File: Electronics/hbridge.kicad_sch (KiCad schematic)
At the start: 24 parts

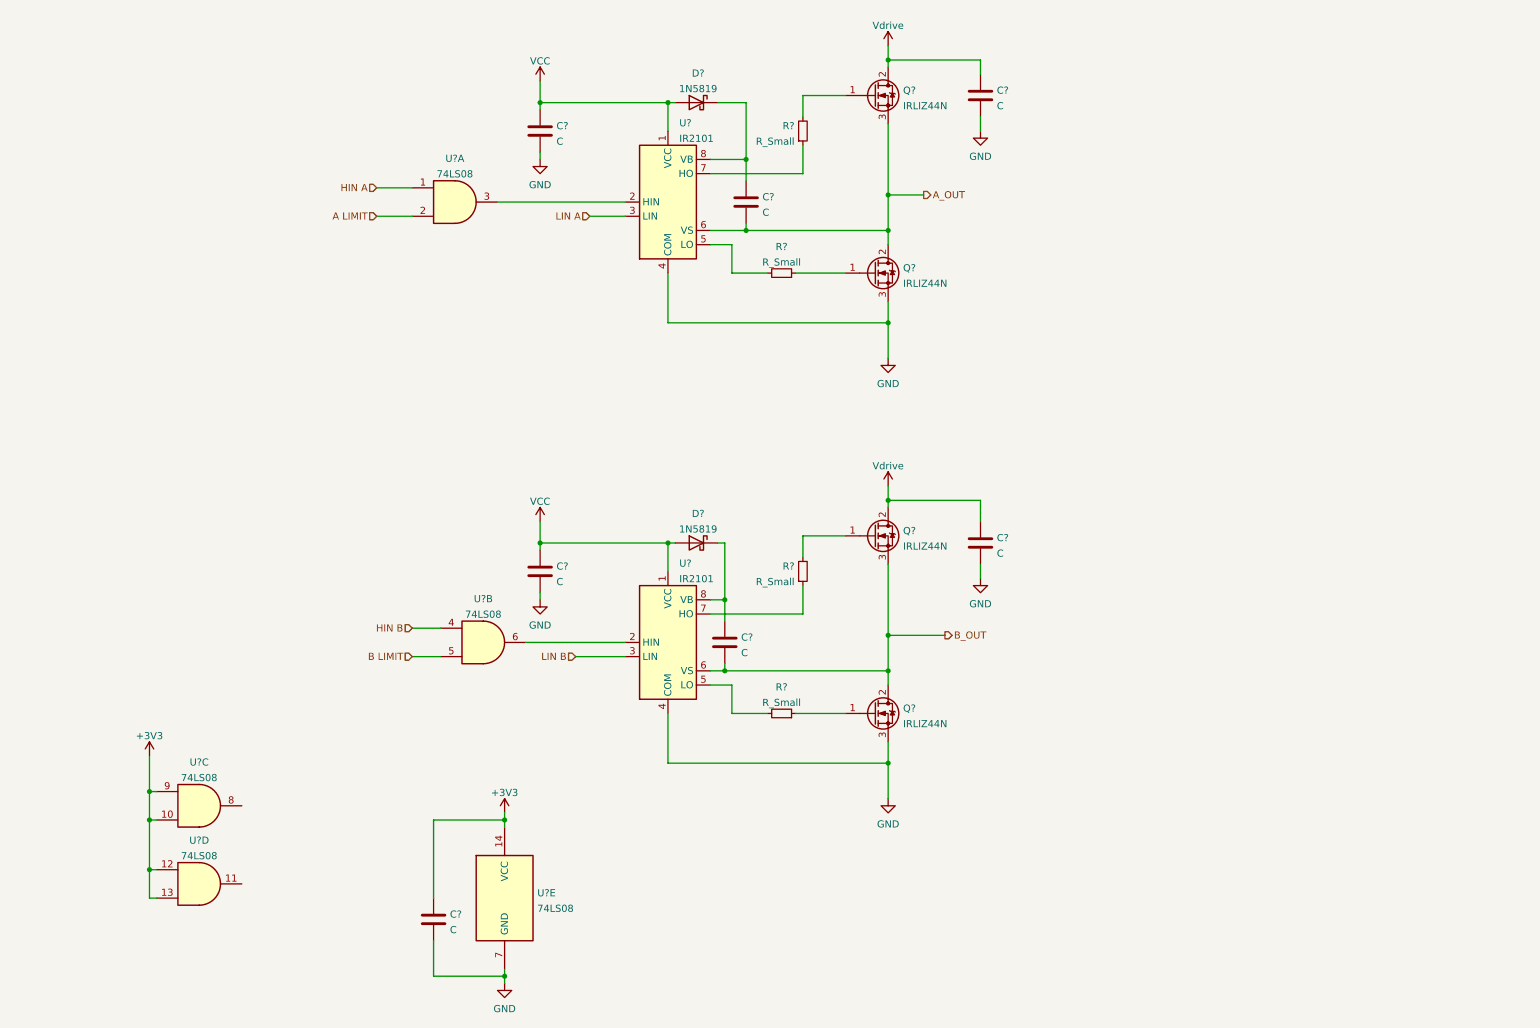
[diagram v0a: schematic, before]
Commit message: Added third half bridge for BLDC applications
Signed-off-by: Finder <aki.kuusela@findersee.fi>
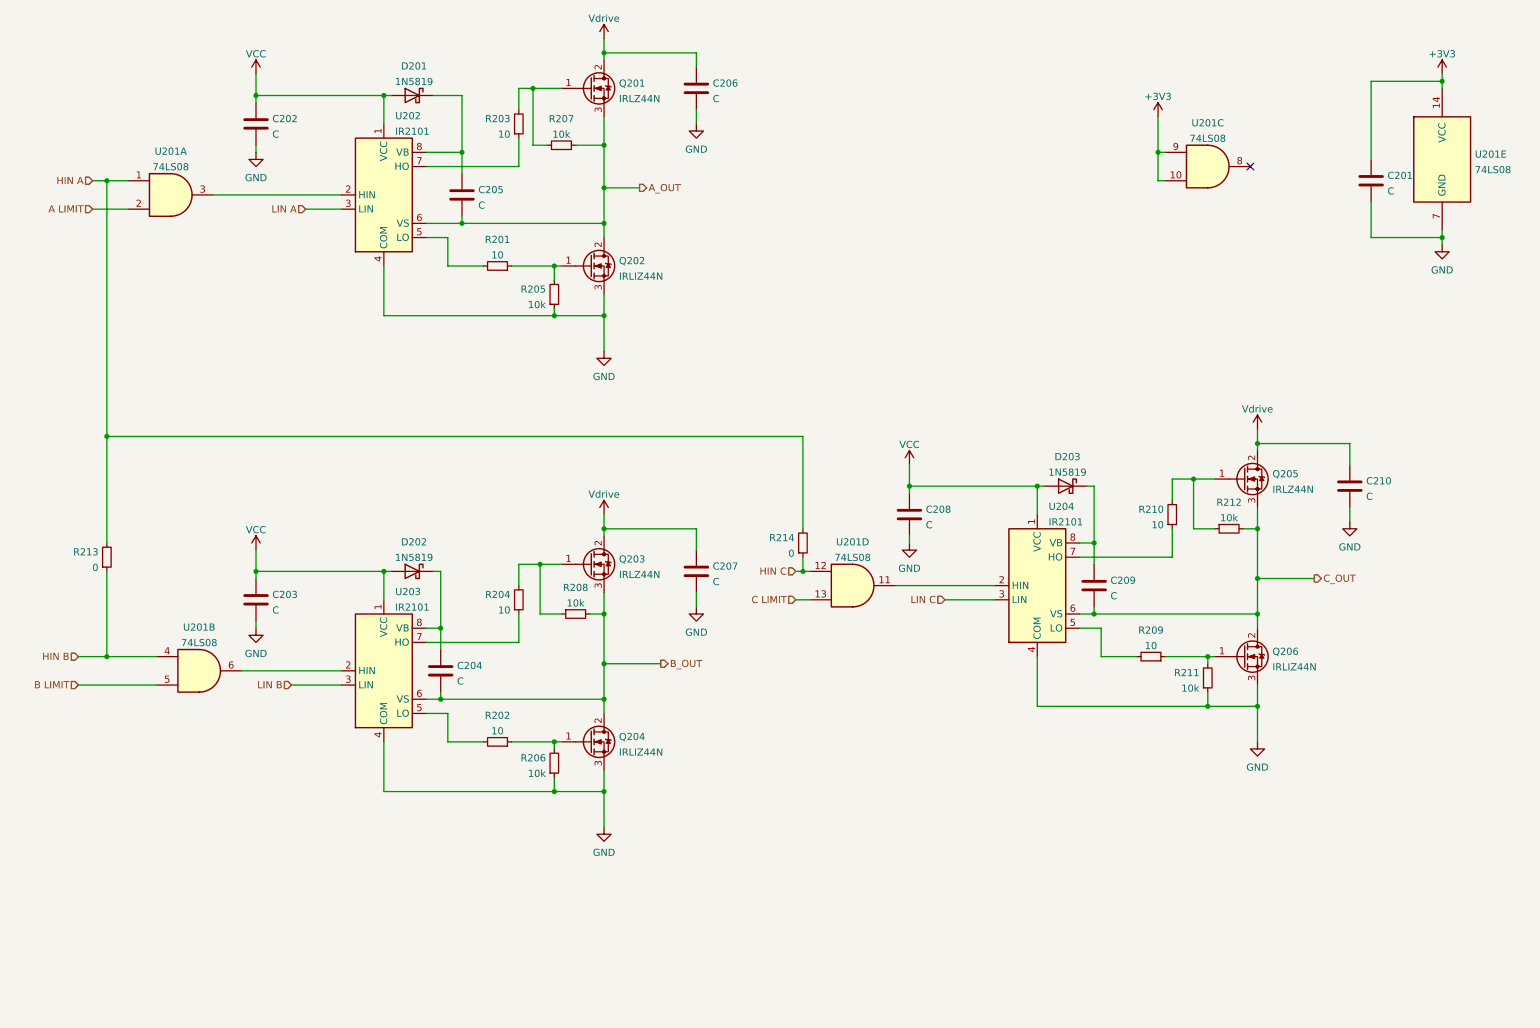
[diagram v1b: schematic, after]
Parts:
- removed Q? (x2): IRLIZ44N, Package_TO_SOT_THT:TO-220F-3_Vertical, symbol Transistor_FET:IRLIZ44N
- added C208, C209: C, Capacitor_SMD:C_0603_1608Metric_Pad1.08x0.95mm_HandSolder, symbol Device:C
- added C210: C, Capacitor_THT:CP_Radial_D10.0mm_P5.00mm, symbol Device:C
- added D203: 1N5819, Diode_SMD:D_SOD-123, symbol Diode:1N5819
- added Q201, Q203, Q205: IRLZ44N, Package_TO_SOT_THT:TO-220-3_Vertical, symbol Transistor_FET:IRLZ44N
- added Q206: IRLIZ44N, Package_TO_SOT_THT:TO-220F-3_Vertical, symbol Transistor_FET:IRLIZ44N
- added R205, R206, R207, R208, R211, R212: 10k, Resistor_SMD:R_0805_2012Metric_Pad1.20x1.40mm_HandSolder, symbol Device:R_Small
- added R209, R210: 10, Resistor_SMD:R_0805_2012Metric_Pad1.20x1.40mm_HandSolder, symbol Device:R_Small
- added R213, R214: 0, Resistor_SMD:R_0805_2012Metric_Pad1.20x1.40mm_HandSolder, symbol Device:R_Small
- added U204: IR2101, Package_SO:SO-8_3.9x4.9mm_P1.27mm, symbol Driver_FET:IR2101
- C201, C202, C203, C204, C205: renamed from C?; footprint (none) -> Capacitor_SMD:C_0603_1608Metric_Pad1.08x0.95mm_HandSolder
- C206, C207: renamed from C?; footprint (none) -> Capacitor_THT:CP_Radial_D10.0mm_P5.00mm
- D201, D202: renamed from D?; footprint Diode_THT:D_DO-41_SOD81_P10.16mm_Horizontal -> Diode_SMD:D_SOD-123
- R201, R202, R203, R204: renamed from R?; value R_Small -> 10; footprint (none) -> Resistor_SMD:R_0805_2012Metric_Pad1.20x1.40mm_HandSolder
- U201: renamed from U?; footprint (none) -> Package_SO:SO-14_3.9x8.65mm_P1.27mm
- U202, U203: renamed from U?; footprint (none) -> Package_SO:SO-8_3.9x4.9mm_P1.27mm
- gave numbers to parts that had none: 2
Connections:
- net +3V3: no longer U201.12, U201.13
- net A_OUT: now also Q201.3 (S), R207.1
- net B_OUT: now also Q203.3 (S), R208.2
- net GND: now also C208.1, C210.2, Q206.3 (S), R205.1, R206.1, R211.1, U204.4 (COM)
- net HIN A: now also R213.2, R214.2
- net HIN B: now also R213.1
- net VCC: now also C208.2, D203.2 (A), U204.1 (VCC)
- net Vdrive: now also C210.1, Q201.2 (D), Q203.2 (D), Q205.2 (D)
- net at R203.2: now also Q201.1 (G), R207.2
- net at Q202.1 (G), R201.1: now also R205.2
- net at R204.2: now also Q203.1 (G), R208.1
- net at U201.11: now also U204.2 (HIN)
- net at Q204.1 (G), R202.1: now also R206.2
- new net: Q205.1 (G), R210.2, R212.1
- new net: R210.1, U204.7 (HO)
- new net: C209.2, D203.1 (K), U204.8 (VB)
- new net: R209.2, U204.5 (LO)
- new net: Q206.1 (G), R209.1, R211.2
- new net C LIMIT: U201.13
- new net C_OUT: C209.1, Q205.3 (S), Q206.2 (D), R212.2, U204.6 (VS)
- new net HIN C: R214.1, U201.12
- new net LIN C: U204.3 (LIN)
- no-connect marks 0 -> 1
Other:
- moved on the sheet: C201, C202, C203, C204, C205, C206, C207, D201, D202, Q202, Q204, R201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

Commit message: Layout update
Signed-off-by: Aki Kuusela <git@findersee.fi>
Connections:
- net +3V3: now also U201.12, U201.13; no longer U201.10, U201.9
- net B LIMIT: now also U201.10; no longer U201.5
- net C LIMIT: now also U201.5; no longer U201.13
- net HIN B: now also U201.9; no longer U201.4
- net HIN C: now also U201.4; no longer U201.12
- net at U201.6: now also U204.2 (HIN); no longer U203.2 (HIN)
- net at U201.11: no longer U204.2 (HIN)
- net at U201.8: now also U203.2 (HIN)
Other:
- moved on the sheet: U201B, U201C, U201D

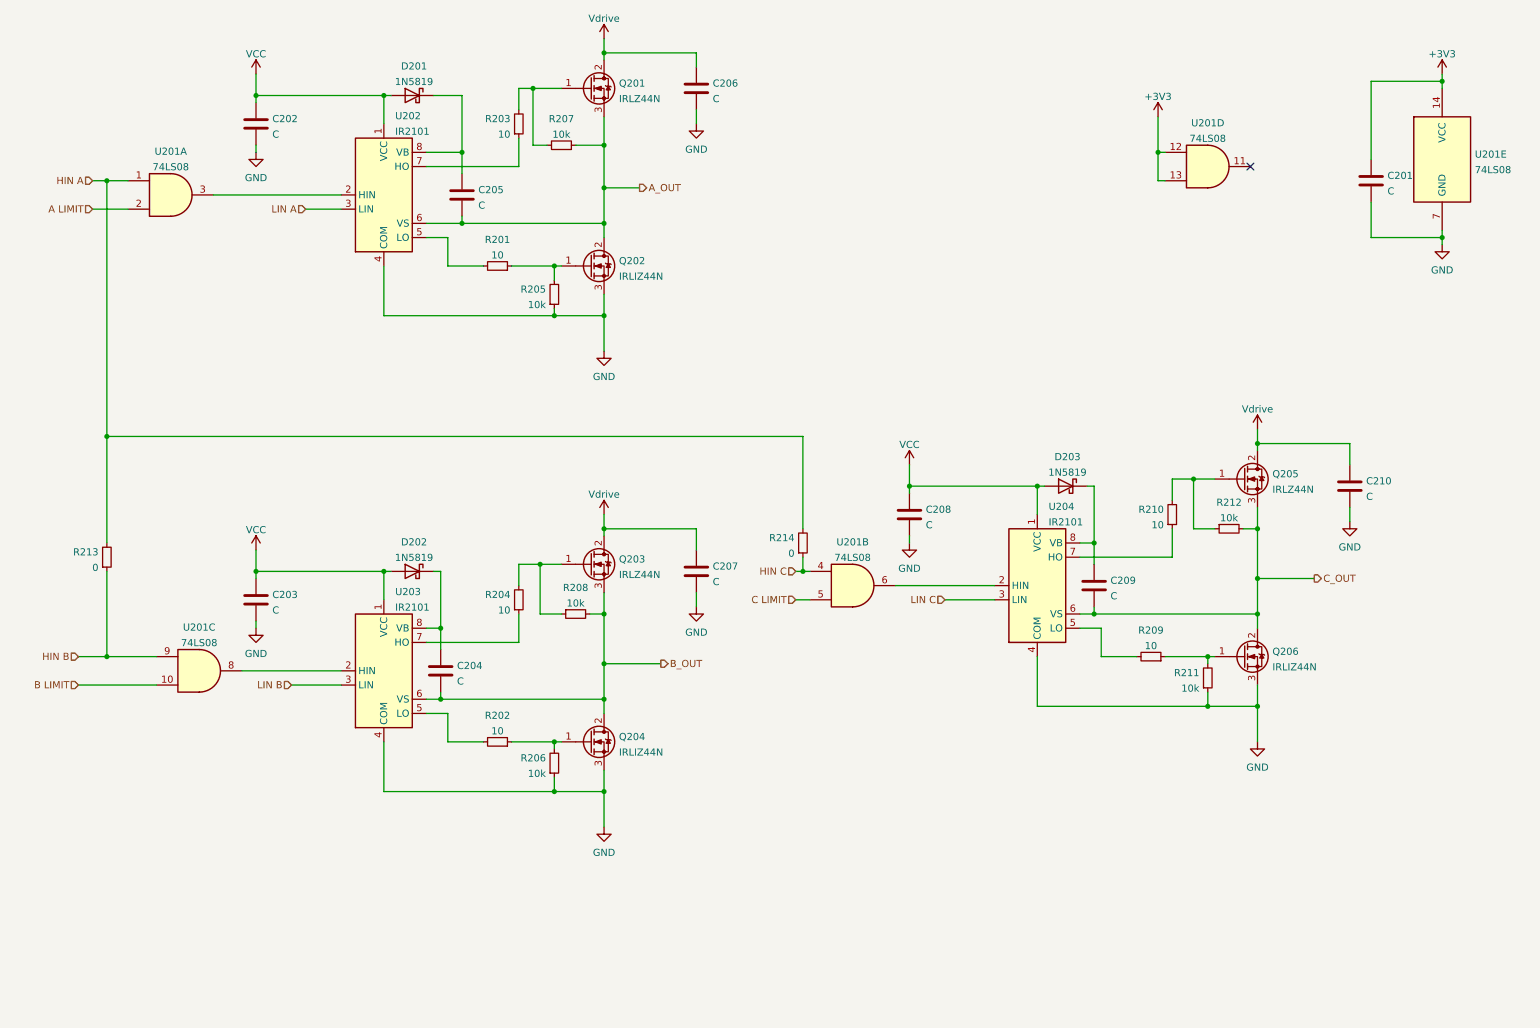
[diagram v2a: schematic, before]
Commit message: Added hall sensor circuitry
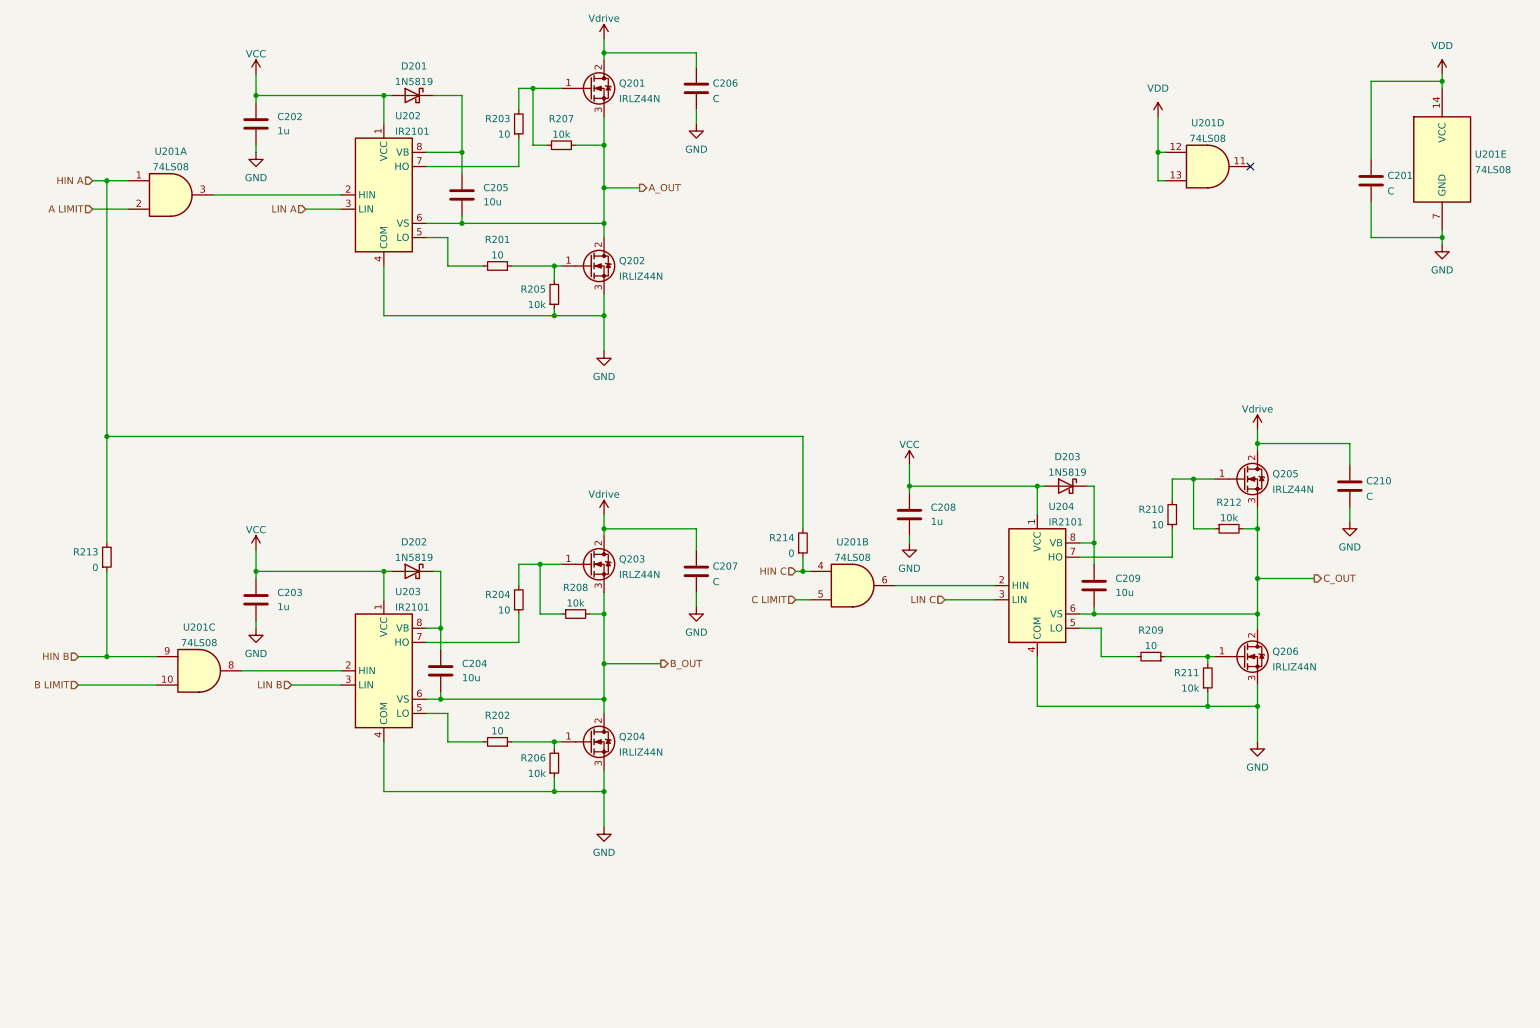
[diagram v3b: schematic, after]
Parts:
- C202, C203, C208: value C -> 1u
- C204, C205, C209: value C -> 10u
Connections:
- net +3V3 renamed VDD
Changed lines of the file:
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@@
   (symbol (lib_id "Device:C") (at 54.61 33.02 180) (unit 1)
     (in_bom yes) (on_board yes) (fields_autoplaced)
-    (property "Reference" "C202" (id 0) (at 57.531 32.1115 0)
-      (effects (font (size 1.27 1.27)) (justify right))
-    )
-    (property "Value" "C" (id 1) (at 57.531 34.8866 0)
+    (property "Reference" "C202" (id 0) (at 58.42 31.7499 0)
+      (effects (font (size 1.27 1.27)) (justify right))
+    )
+    (property "Value" "1u" (id 1) (at 58.42 34.2899 0)
       (effects (font (size 1.27 1.27)) (justify right))
     )
@@
   (symbol (lib_id "Device:C") (at 87.63 130.81 180) (unit 1)
     (in_bom yes) (on_board yes) (fields_autoplaced)
-    (property "Reference" "C204" (id 0) (at 90.551 129.9015 0)
-      (effects (font (size 1.27 1.27)) (justify right))
-    )
-    (property "Value" "C" (id 1) (at 90.551 132.6766 0)
+    (property "Reference" "C204" (id 0) (at 91.44 129.5399 0)
+      (effects (font (size 1.27 1.27)) (justify right))
+    )
+    (property "Value" "10u" (id 1) (at 91.44 132.0799 0)
       (effects (font (size 1.27 1.27)) (justify right))
     )
@@
     (pin "1")
     (pin "2")
-  )
-  (symbol (lib_id "power:+3V3") (at 215.9 31.75 0) (unit 1)
-    (in_bom yes) (on_board yes) (fields_autoplaced)
-    (property "Reference" "#PWR0111" (id 0) (at 215.9 35.56 0)
-      (effects (font (size 1.27 1.27)) hide)
-    )
-    (property "Value" "+3V3" (id 1) (at 215.9 28.1455 0))
-    (property "Footprint" "" (id 2) (at 215.9 31.75 0)
-      (effects (font (size 1.27 1.27)) hide)
-    )
-    (property "Datasheet" "" (id 3) (at 215.9 31.75 0)
-      (effects (font (size 1.27 1.27)) hide)
-    )
-    (pin "1")
   )
   (symbol (lib_id "Transistor_FET:IRLZ44N") (at 231.14 96.52 0) (unit 1)
@@
     )
     (property "Datasheet" "" (id 3) (at 54.61 38.1 0)
-      (effects (font (size 1.27 1.27)) hide)
-    )
-    (pin "1")
-  )
-  (symbol (lib_id "power:+3V3") (at 266.7 24.13 0) (unit 1)
-    (in_bom yes) (on_board yes) (fields_autoplaced)
-    (property "Reference" "#PWR0109" (id 0) (at 266.7 27.94 0)
-      (effects (font (size 1.27 1.27)) hide)
-    )
-    (property "Value" "+3V3" (id 1) (at 266.7 20.5255 0))
-    (property "Footprint" "" (id 2) (at 266.7 24.13 0)
-      (effects (font (size 1.27 1.27)) hide)
-    )
-    (property "Datasheet" "" (id 3) (at 266.7 24.13 0)
       (effects (font (size 1.27 1.27)) hide)
     )
@@
   (symbol (lib_id "Device:C") (at 204.47 115.57 180) (unit 1)
     (in_bom yes) (on_board yes) (fields_autoplaced)
-    (property "Reference" "C209" (id 0) (at 207.391 114.6615 0)
-      (effects (font (size 1.27 1.27)) (justify right))
-    )
-    (property "Value" "C" (id 1) (at 207.391 117.4366 0)
+    (property "Reference" "C209" (id 0) (at 208.28 114.2999 0)
+      (effects (font (size 1.27 1.27)) (justify right))
+    )
+    (property "Value" "10u" (id 1) (at 208.28 116.8399 0)
       (effects (font (size 1.27 1.27)) (justify right))
     )
@@
   (symbol (lib_id "Device:C") (at 171.45 102.87 180) (unit 1)
     (in_bom yes) (on_board yes) (fields_autoplaced)
-    (property "Reference" "C208" (id 0) (at 174.371 101.9615 0)
-      (effects (font (size 1.27 1.27)) (justify right))
-    )
-    (property "Value" "C" (id 1) (at 174.371 104.7366 0)
+    (property "Reference" "C208" (id 0) (at 175.26 101.5999 0)
+      (effects (font (size 1.27 1.27)) (justify right))
+    )
+    (property "Value" "1u" (id 1) (at 175.26 104.1399 0)
       (effects (font (size 1.27 1.27)) (justify right))
     )
@@
   (symbol (lib_id "Device:C") (at 91.44 45.72 180) (unit 1)
     (in_bom yes) (on_board yes) (fields_autoplaced)
-    (property "Reference" "C205" (id 0) (at 94.361 44.8115 0)
-      (effects (font (size 1.27 1.27)) (justify right))
-    )
-    (property "Value" "C" (id 1) (at 94.361 47.5866 0)
+    (property "Reference" "C205" (id 0) (at 95.25 44.4499 0)
+      (effects (font (size 1.27 1.27)) (justify right))
+    )
+    (property "Value" "10u" (id 1) (at 95.25 46.9899 0)
       (effects (font (size 1.27 1.27)) (justify right))
     )
@@
     (pin "2")
   )
+  (symbol (lib_id "power:VDD") (at 266.7 24.13 0) (unit 1)
+    (in_bom yes) (on_board yes) (fields_autoplaced)
+    (property "Reference" "#PWR0109" (id 0) (at 266.7 27.94 0)
+      (effects (font (size 1.27 1.27)) hide)
+    )
+    (property "Value" "VDD" (id 1) (at 266.7 19.05 0))
+    (property "Footprint" "" (id 2) (at 266.7 24.13 0)
+      (effects (font (size 1.27 1.27)) hide)
+    )
+    (property "Datasheet" "" (id 3) (at 266.7 24.13 0)
+      (effects (font (size 1.27 1.27)) hide)
+    )
+    (pin "1")
+  )
   (symbol (lib_id "power:GND") (at 133.35 119.38 0) (unit 1)
     (in_bom yes) (on_board yes) (fields_autoplaced)
@@
     (pin "1")
     (pin "2")
+  )
+  (symbol (lib_id "power:VDD") (at 215.9 31.75 0) (unit 1)
+    (in_bom yes) (on_board yes) (fields_autoplaced)
+    (property "Reference" "#PWR0111" (id 0) (at 215.9 35.56 0)
+      (effects (font (size 1.27 1.27)) hide)
+    )
+    (property "Value" "VDD" (id 1) (at 215.9 26.67 0))
+    (property "Footprint" "" (id 2) (at 215.9 31.75 0)
+      (effects (font (size 1.27 1.27)) hide)
+    )
+    (property "Datasheet" "" (id 3) (at 215.9 31.75 0)
+      (effects (font (size 1.27 1.27)) hide)
+    )
+    (pin "1")
   )
   (symbol (lib_id "Device:R_Small") (at 101.6 33.02 0) (mirror x) (unit 1)
@@
   (symbol (lib_id "Device:C") (at 54.61 118.11 180) (unit 1)
     (in_bom yes) (on_board yes) (fields_autoplaced)
-    (property "Reference" "C203" (id 0) (at 57.531 117.2015 0)
-      (effects (font (size 1.27 1.27)) (justify right))
-    )
-    (property "Value" "C" (id 1) (at 57.531 119.9766 0)
-      (effects (font (size 1.27 1.27)) (justify right))
-    )
+    (property "Reference" "C203" (id 0) (at 58.42 116.8399 0)
+      (effects (font (size 1.27 1.27)) (justify right))
+    )
+    (property "Value" "1u" (id 1) (at 58.42 119.3799 0)
+      (effects (font (size 1.27 1.27)) (justify right))
+    )
